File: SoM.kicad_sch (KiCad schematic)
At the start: 0 parts

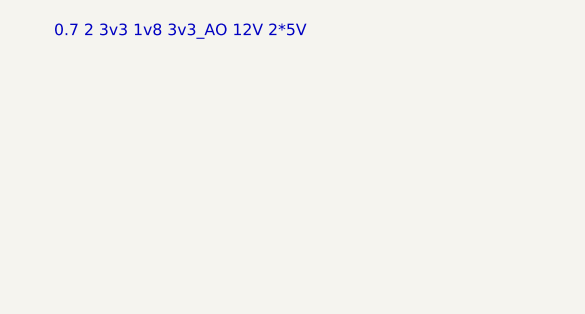
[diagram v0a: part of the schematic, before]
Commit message: [#81778] Rename power label
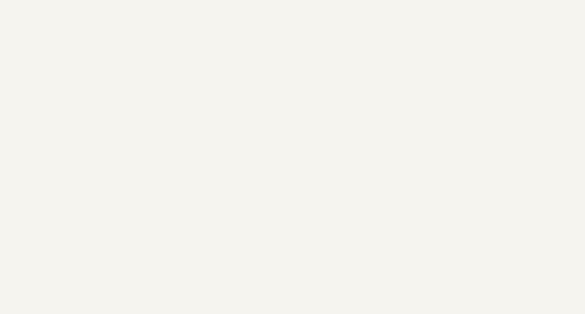
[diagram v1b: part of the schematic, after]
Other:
- note removed: "0.7 2 3v3 1v8 3v3_AO 12V 2*5V"
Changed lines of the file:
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@@
 		(comment 1 "www.antmicro.com")
-	)
-	(text "0.7 2 3v3 1v8 3v3_AO 12V 2*5V"
-		(exclude_from_sim no)
-		(at 126.746 -93.98 0)
-		(effects
-			(font
-				(size 1.27 1.27)
-			)
-		)
 	)
 	(sheet
